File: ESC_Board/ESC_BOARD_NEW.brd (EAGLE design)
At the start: 127.7 x 178 mm, 165 parts, among them J3 AVR_SPI_PROG_3X2NS, U2 ATMEGA328P_TQFP, U4 PCA9685

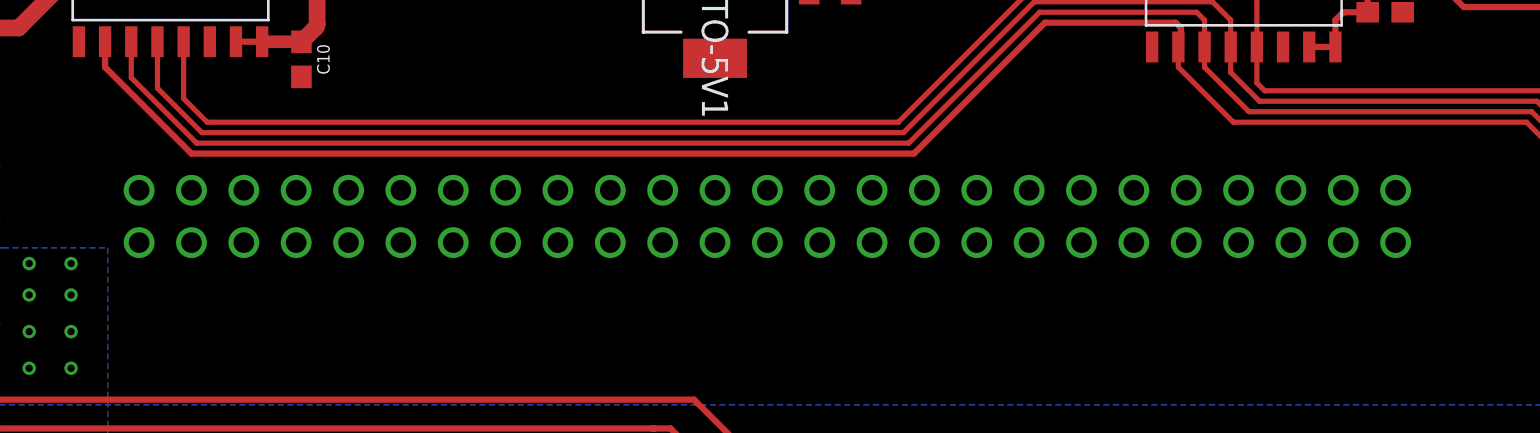
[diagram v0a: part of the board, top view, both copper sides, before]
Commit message: Added standard ESC to power distribution board connector
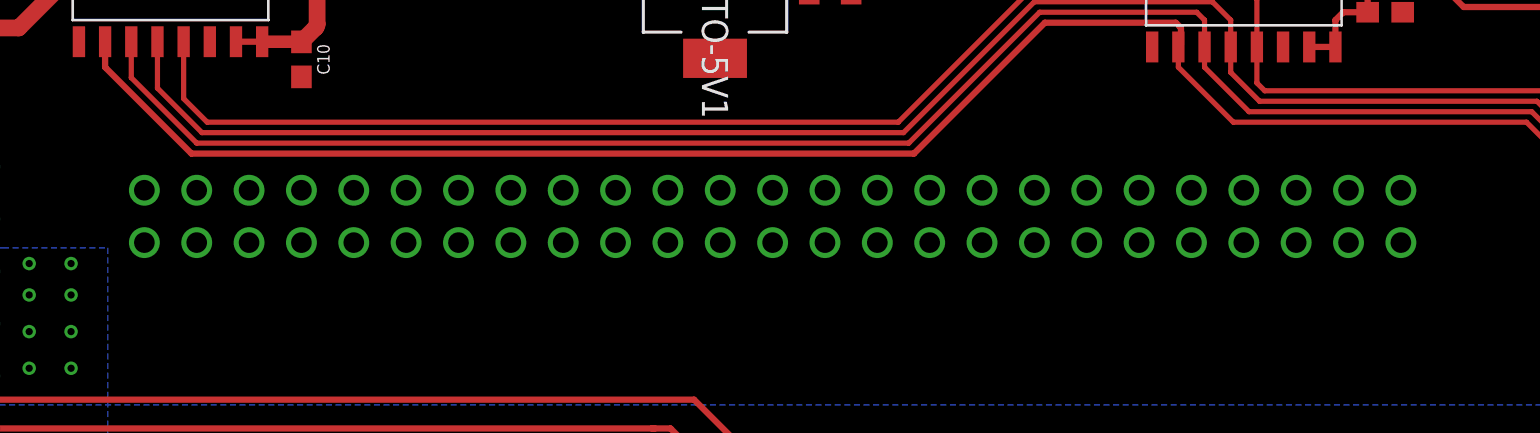
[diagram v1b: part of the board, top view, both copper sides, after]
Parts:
- removed U$17, U$18: POWER-BRICK-CONNECTOR, MotherboardParts:POWER-BRICK-CONNECTOR
- added U$14: ESC-CONNECTORESC-CONNECTOR, MotherboardParts:ESC-CONNECTOR
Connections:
- net +12V: now also U$14.P$100, U$14.P$51, U$14.P$52, U$14.P$53, U$14.P$54, U$14.P$55, U$14.P$56, U$14.P$57, U$14.P$58, U$14.P$59, U$14.P$60, U$14.P$61, U$14.P$62, U$14.P$63, U$14.P$64, U$14.P$65, U$14.P$66, U$14.P$67, U$14.P$68, U$14.P$69, U$14.P$70, U$14.P$71, U$14.P$72, U$14.P$73, U$14.P$74, U$14.P$75, U$14.P$76, U$14.P$77, U$14.P$78, U$14.P$79, U$14.P$80, U$14.P$81, U$14.P$82, U$14.P$83, U$14.P$84, U$14.P$85, U$14.P$86, U$14.P$87, U$14.P$88, U$14.P$89, U$14.P$90, U$14.P$91, U$14.P$92, U$14.P$93, U$14.P$94, U$14.P$95, U$14.P$96, U$14.P$97, U$14.P$98, U$14.P$99; no longer U$18.P$1, U$18.P$10, U$18.P$11, U$18.P$12, U$18.P$13, U$18.P$14, U$18.P$15, U$18.P$16, U$18.P$17, U$18.P$18, U$18.P$19, U$18.P$2, U$18.P$20, U$18.P$21, U$18.P$22, U$18.P$23, U$18.P$24, U$18.P$25, U$18.P$26, U$18.P$27, U$18.P$28, U$18.P$29, U$18.P$3, U$18.P$30, U$18.P$31, U$18.P$32, U$18.P$33, U$18.P$34, U$18.P$35, U$18.P$36, U$18.P$37, U$18.P$38, U$18.P$39, U$18.P$4, U$18.P$40, U$18.P$41, U$18.P$42, U$18.P$43, U$18.P$44, U$18.P$45, U$18.P$46, U$18.P$47, U$18.P$48, U$18.P$49, U$18.P$5, U$18.P$50, U$18.P$6, U$18.P$7, U$18.P$8, U$18.P$9
- net GND: now also U$14.P$1, U$14.P$10, U$14.P$11, U$14.P$12, U$14.P$13, U$14.P$14, U$14.P$15, U$14.P$16, U$14.P$17, U$14.P$18, U$14.P$19, U$14.P$2, U$14.P$20, U$14.P$21, U$14.P$22, U$14.P$23, U$14.P$24, U$14.P$25, U$14.P$26, U$14.P$27, U$14.P$28, U$14.P$29, U$14.P$3, U$14.P$30, U$14.P$31, U$14.P$32, U$14.P$33, U$14.P$34, U$14.P$35, U$14.P$36, U$14.P$37, U$14.P$38, U$14.P$39, U$14.P$4, U$14.P$40, U$14.P$41, U$14.P$42, U$14.P$43, U$14.P$44, U$14.P$45, U$14.P$46, U$14.P$47, U$14.P$48, U$14.P$49, U$14.P$5, U$14.P$50, U$14.P$6, U$14.P$7, U$14.P$8, U$14.P$9; no longer U$17.P$1, U$17.P$10, U$17.P$11, U$17.P$12, U$17.P$13, U$17.P$14, U$17.P$15, U$17.P$16, U$17.P$17, U$17.P$18, U$17.P$19, U$17.P$2, U$17.P$20, U$17.P$21, U$17.P$22, U$17.P$23, U$17.P$24, U$17.P$25, U$17.P$26, U$17.P$27, U$17.P$28, U$17.P$29, U$17.P$3, U$17.P$30, U$17.P$31, U$17.P$32, U$17.P$33, U$17.P$34, U$17.P$35, U$17.P$36, U$17.P$37, U$17.P$38, U$17.P$39, U$17.P$4, U$17.P$40, U$17.P$41, U$17.P$42, U$17.P$43, U$17.P$44, U$17.P$45, U$17.P$46, U$17.P$47, U$17.P$48, U$17.P$49, U$17.P$5, U$17.P$50, U$17.P$6, U$17.P$7, U$17.P$8, U$17.P$9

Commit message: Some final changes
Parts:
- U$14: value ESC-CONNECTORESC-CONNECTOR -> ESC-CONNECTORPARALLELL; device MotherboardParts:ESC-CONNECTOR -> MotherboardParts:ESC-PARALLELL
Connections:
- net +12V: now also U$14.P$101, U$14.P$102, U$14.P$103, U$14.P$104, U$14.P$105, U$14.P$106, U$14.P$107, U$14.P$108, U$14.P$109, U$14.P$110, U$14.P$111, U$14.P$112, U$14.P$113, U$14.P$114, U$14.P$115, U$14.P$116, U$14.P$117, U$14.P$118, U$14.P$119, U$14.P$120, U$14.P$121, U$14.P$122, U$14.P$123, U$14.P$124, U$14.P$125, U$14.P$126, U$14.P$127, U$14.P$128, U$14.P$129, U$14.P$130; no longer U$14.P$100, U$14.P$81, U$14.P$82, U$14.P$83, U$14.P$84, U$14.P$85, U$14.P$86, U$14.P$87, U$14.P$88, U$14.P$89, U$14.P$90, U$14.P$91, U$14.P$92, U$14.P$93, U$14.P$94, U$14.P$95, U$14.P$96, U$14.P$97, U$14.P$98, U$14.P$99
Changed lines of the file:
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@@
 <element name="LED8" library="microbuilder" package="WS2812B" value="WS2812B5050" x="85.852" y="22.352" rot="R270"/>
 <element name="C8" library="rcl" library_urn="urn:adsk.eagle:library:334" package="C0603" package3d_urn="urn:adsk.eagle:package:23616/2" value="0.1uF" x="88.138" y="18.034" rot="MR180"/>
-<element name="U$14" library="MotherboardParts" package="ESC-CONNECTOR" value="ESC-CONNECTORESC-CONNECTOR" x="55.372" y="173.736" rot="R90"/>
+<element name="U$14" library="MotherboardParts" package="ESC-PARALLELL" value="ESC-CONNECTORPARALLELL" x="55.372" y="173.736" rot="R90"/>
 </elements>
 <signals>
@@
 <contactref element="U$16" pad="P$8"/>
 <contactref element="U$16" pad="P$9"/>
-<contactref element="U$14" pad="P$85"/>
+<contactref element="U$14" pad="P$105"/>
 <contactref element="U$14" pad="P$73"/>
 <contactref element="U$14" pad="P$77"/>
@@
 <contactref element="U$14" pad="P$79"/>
 <contactref element="U$14" pad="P$66"/>
-<contactref element="U$14" pad="P$82"/>
-<contactref element="U$14" pad="P$81"/>
+<contactref element="U$14" pad="P$102"/>
+<contactref element="U$14" pad="P$101"/>
 <contactref element="U$14" pad="P$55"/>
 <contactref element="U$14" pad="P$60"/>
-<contactref element="U$14" pad="P$97"/>
-<contactref element="U$14" pad="P$87"/>
-<contactref element="U$14" pad="P$99"/>
-<contactref element="U$14" pad="P$83"/>
+<contactref element="U$14" pad="P$117"/>
+<contactref element="U$14" pad="P$107"/>
+<contactref element="U$14" pad="P$119"/>
+<contactref element="U$14" pad="P$103"/>
 <contactref element="U$14" pad="P$78"/>
-<contactref element="U$14" pad="P$94"/>
-<contactref element="U$14" pad="P$98"/>
+<contactref element="U$14" pad="P$114"/>
+<contactref element="U$14" pad="P$118"/>
 <contactref element="U$14" pad="P$75"/>
 <contactref element="U$14" pad="P$64"/>
-<contactref element="U$14" pad="P$89"/>
+<contactref element="U$14" pad="P$109"/>
 <contactref element="U$14" pad="P$56"/>
-<contactref element="U$14" pad="P$95"/>
+<contactref element="U$14" pad="P$115"/>
 <contactref element="U$14" pad="P$71"/>
 <contactref element="U$14" pad="P$68"/>
-<contactref element="U$14" pad="P$90"/>
+<contactref element="U$14" pad="P$110"/>
 <contactref element="U$14" pad="P$63"/>
-<contactref element="U$14" pad="P$84"/>
+<contactref element="U$14" pad="P$104"/>
 <contactref element="U$14" pad="P$61"/>
 <contactref element="U$14" pad="P$69"/>
-<contactref element="U$14" pad="P$92"/>
-<contactref element="U$14" pad="P$100"/>
+<contactref element="U$14" pad="P$112"/>
+<contactref element="U$14" pad="P$120"/>
 <contactref element="U$14" pad="P$54"/>
-<contactref element="U$14" pad="P$96"/>
+<contactref element="U$14" pad="P$116"/>
 <contactref element="U$14" pad="P$80"/>
 <contactref element="U$14" pad="P$67"/>
@@
 <contactref element="U$14" pad="P$70"/>
 <contactref element="U$14" pad="P$72"/>
-<contactref element="U$14" pad="P$91"/>
+<contactref element="U$14" pad="P$111"/>
 <contactref element="U$14" pad="P$52"/>
 <contactref element="U$14" pad="P$65"/>
-<contactref element="U$14" pad="P$86"/>
+<contactref element="U$14" pad="P$106"/>
 <contactref element="U$14" pad="P$51"/>
-<contactref element="U$14" pad="P$93"/>
-<contactref element="U$14" pad="P$88"/>
+<contactref element="U$14" pad="P$113"/>
+<contactref element="U$14" pad="P$108"/>
+<contactref element="U$14" pad="P$121"/>
+<contactref element="U$14" pad="P$122"/>
+<contactref element="U$14" pad="P$123"/>
+<contactref element="U$14" pad="P$124"/>
+<contactref element="U$14" pad="P$125"/>
+<contactref element="U$14" pad="P$126"/>
+<contactref element="U$14" pad="P$127"/>
+<contactref element="U$14" pad="P$128"/>
+<contactref element="U$14" pad="P$129"/>
+<contactref element="U$14" pad="P$130"/>
 </signal>
 <signal name="PWM2">

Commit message: Added way to power electro magnets
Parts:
- added J4, J6: (no value), SparkFun-Connectors:1X02
- added LED10, LED9: (no value), led:SML0603
- added R4, R5: 330, resistor:R0603
- added U1, U3: FQB27P06, CamSensComponents:TO263-3
- moved P7 3.75 mm to (3.81, 35.3)
- moved P6 1.48 mm to (3.81, 37.8)
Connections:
- removed net PWME1: P6.1, U4.12
- removed net PWME2: P7.1, U4.13
- new net E_MAG_1: J4.2, R5.2, U1.TAB
- new net E_MAG_1_ON: P6.1, U1.1, U4.12
- new net E_MAG_2: J6.2, R4.2, U3.TAB
- new net E_MAG_2_ON: P7.1, U3.1, U4.13
- new net N$51: LED9.A, R5.1
- new net N$64: LED10.A, R4.1
- net +12V: now also U1.3, U3.3
- net GND: now also J4.1, J6.1, LED10.C, LED9.C
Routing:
- net E_MAG_1_ON: track 0.00 -> 83.0 mm, vias 0 -> 1
- net E_MAG_2_ON: track 0.00 -> 74.9 mm
- net E_MAG_1: track 0.00 -> 32.2 mm
- net E_MAG_2: track 0.00 -> 20.1 mm
- net PWME2: track 8.69 -> 0.00 mm
- net PWME1: track 6.06 -> 0.00 mm
- net +12V: track 0.00 -> 2.29 mm, vias 11 -> 12
- net N$51: track 0.00 -> 1.96 mm
- net N$64: track 0.00 -> 1.70 mm
- net MOSI: track 162.5 -> 161.6 mm
- net +5V: track 766.0 -> 765.1 mm
- net GND: vias 96 -> 105

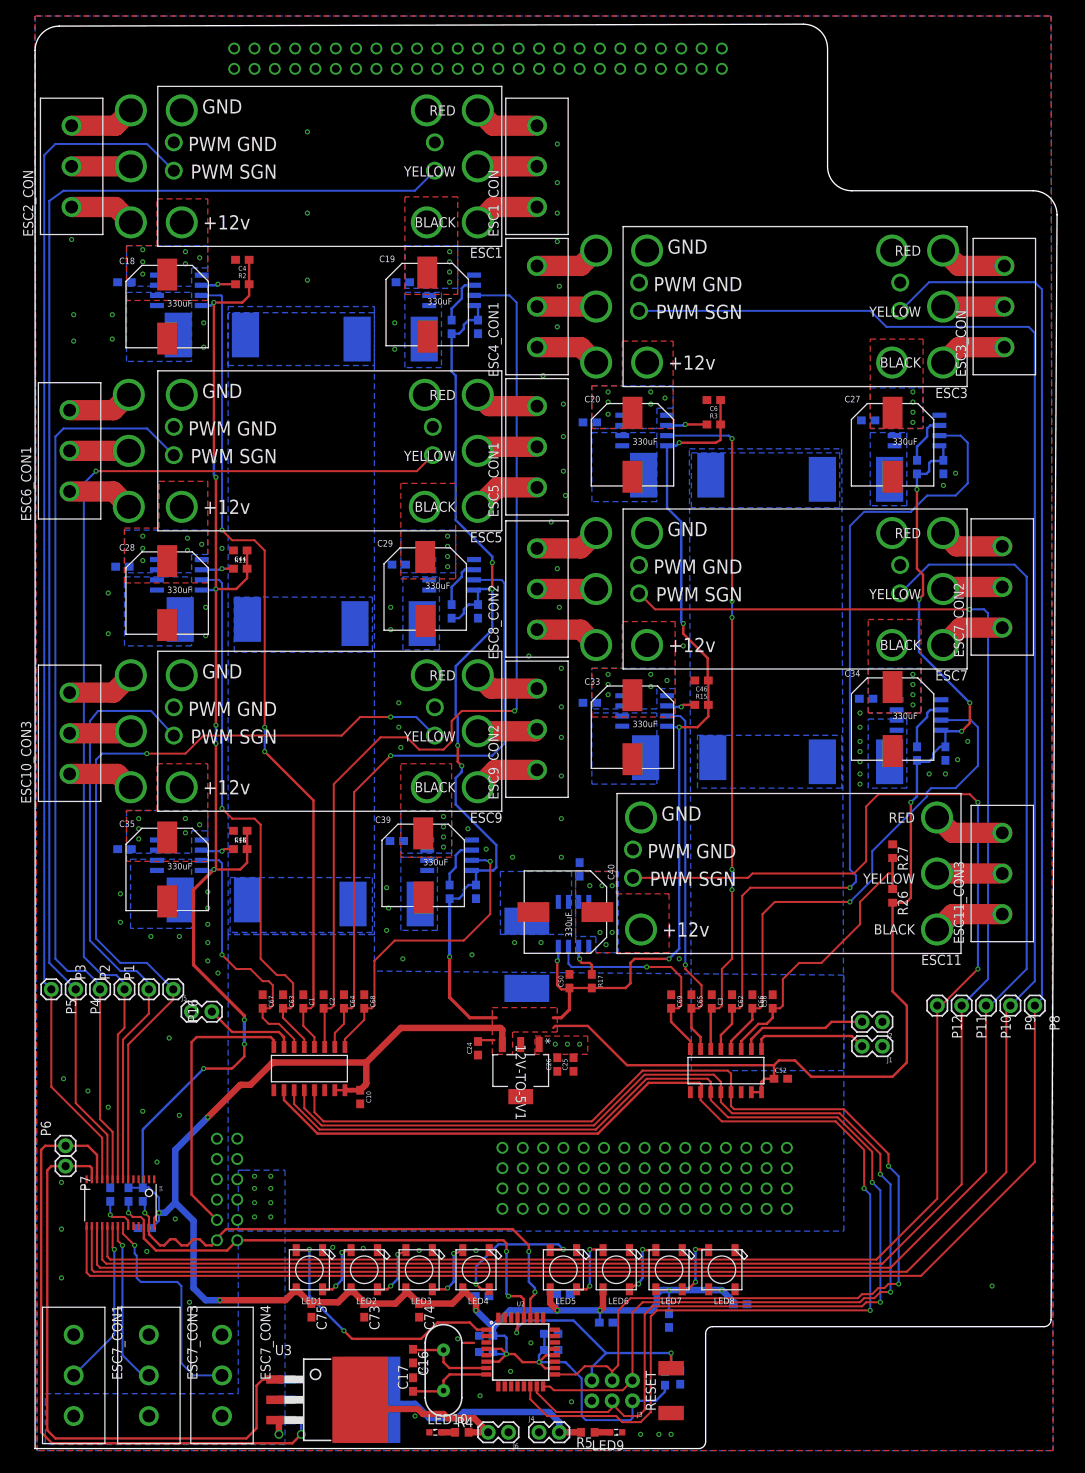
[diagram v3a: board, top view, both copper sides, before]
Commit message: fixed up some of ground plane
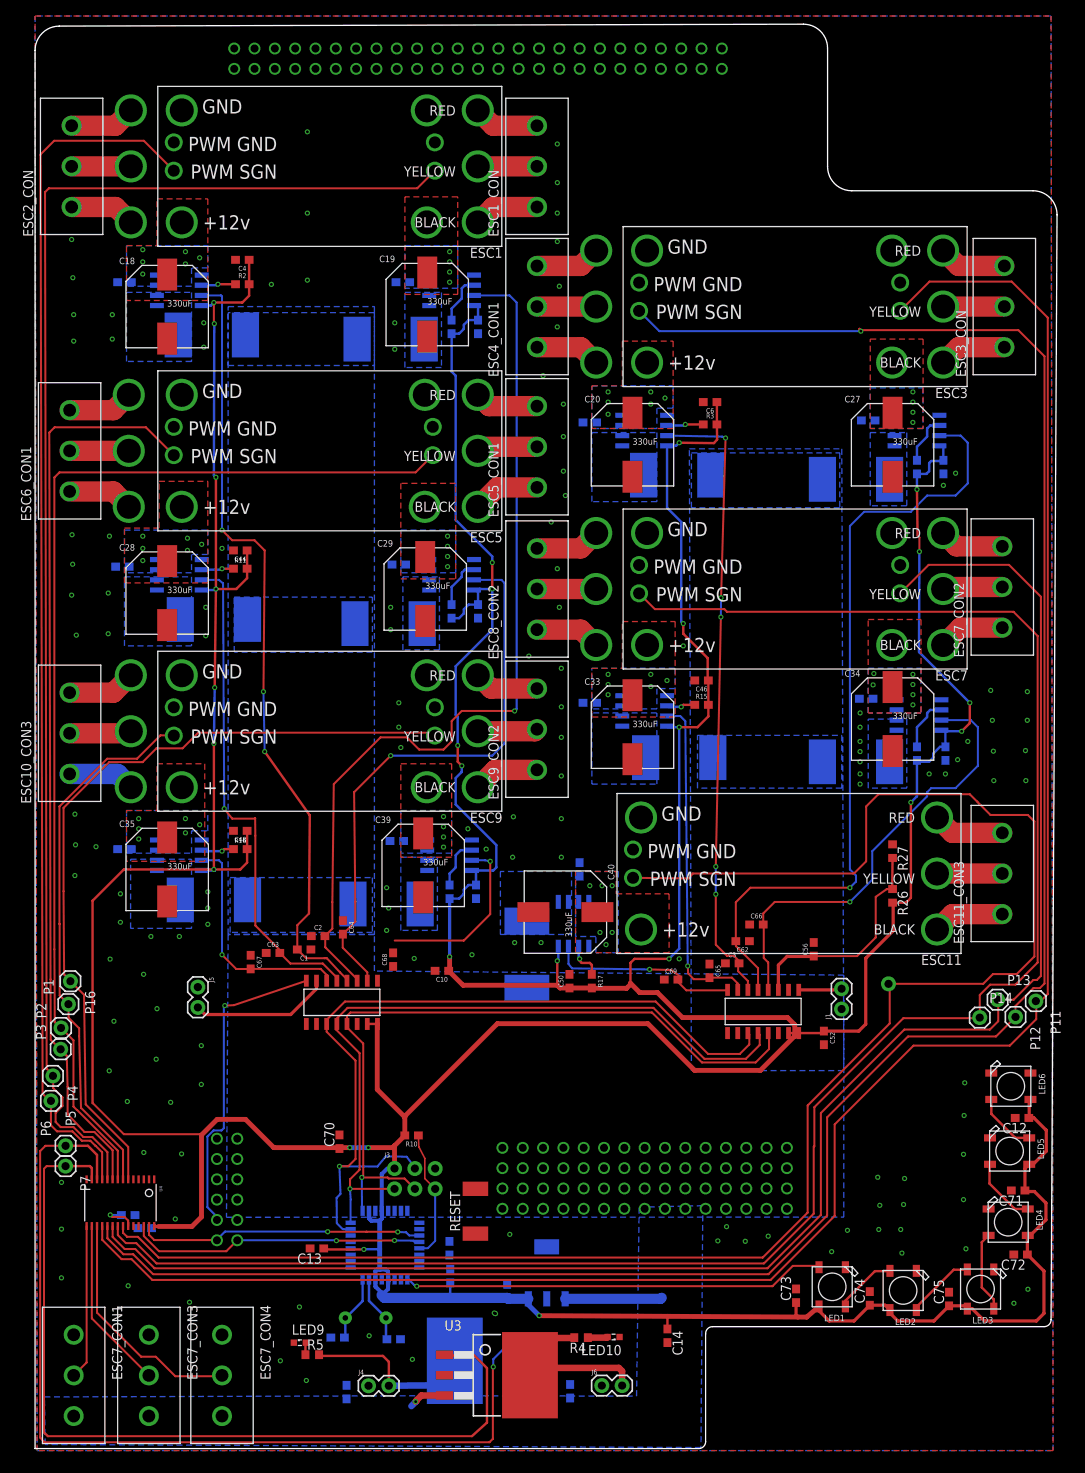
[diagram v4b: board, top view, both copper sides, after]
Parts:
- removed C7, C8: 0.1uF, rcl:C0603
- removed J2: (no value), SparkFun-Connectors:1X02
- removed LED7, LED8: WS2812B5050, microbuilder:WS2812B
- removed P10, P8, P9: (no value), SparkFun-Connectors:1X01
- removed R20, R21: 10k, SparkFun-Resistors:0603-RES
- added P13, P14, P15: (no value), SparkFun-Connectors:1X01
- moved C75 79.7 mm to (114.2, 18.7), turned to 90 degrees
- moved C12 72.3 mm to (123.4, 41.3), flipped to the top, turned to 180 degrees
- moved LED3 70.2 mm to (118.2, 19.9)
- moved C71 68.3 mm to (122.9, 32.3), flipped to the top
- moved LED2 67.4 mm to (108.5, 19.8)
- moved LED4 66.8 mm to (121.6, 28.3), turned to 0 degrees
- moved LED1 65.4 mm to (99.6, 20.2)
- moved LED5 57.7 mm to (121.8, 37.2), turned to 0 degrees
- moved C74 56.4 mm to (104.3, 18.8), turned to 90 degrees
- moved LED6 54.4 mm to (122.0, 45.3), turned to 0 degrees
- moved C73 54.0 mm to (95.1, 19.1), turned to 90 degrees
- moved C72 52.5 mm to (123.2, 24.3), flipped to the top
- moved C25 49.8 mm to (38.9, 7.06), flipped to the bottom, turned to 270 degrees
- moved R10 43.9 mm to (47.1, 39.1), flipped to the top, turned to 180 degrees
- moved LED9 41.1 mm to (33.1, 13.2), turned to 0 degrees
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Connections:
- removed net OUT7: LED7.2-DOUT, LED8.4-DIN
- removed net OUT8: LED8.2-DOUT
- net +5V: no longer C7.1, C8.1, LED7.1-VDD, LED8.1-VDD, R20.2, R21.2
- net E4: no longer J2.2
- net GND: no longer C7.2, C8.2, J2.1, LED7.3-GND, LED8.3-GND
- net LED1: now also U4.15; no longer U4.20
- net LED2: now also U4.16; no longer U4.21
- net OUT6: no longer LED7.4-DIN
- net PIEZO: now also U4.17; no longer U4.22
- net PWM11: now also P15.1, U4.22; no longer P12.1, U4.19
- net PWM3: now also P12.1, U4.19; no longer P9.1, U4.16
- net PWM4: now also P11.1, U4.18; no longer P8.1, U4.15
- net PWM7: now also P14.1, U4.21; no longer P11.1, U4.18
- net PWM8: now also P13.1, U4.20; no longer P10.1, U4.17
- net SCL: no longer R21.1
- net SDA: no longer R20.1
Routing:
- net CS: track 161.6 -> 0.00 mm, vias 2 -> 0
- net MISO: track 155.1 -> 91.3 mm, vias 2 -> 1
- net SCK: track 154.4 -> 91.1 mm, vias 2 -> 1
- net MOSI: track 161.6 -> 100.1 mm, vias 2 -> 1
- net E_MAG_1_ON: track 83.0 -> 120.6 mm
- net E_MAG_2_ON: track 74.9 -> 109.6 mm
- net SDA: track 65.3 -> 35.9 mm, vias 3 -> 2
- net +5V: track 765.1 -> 792.1 mm, vias 35 -> 26
- net SCL: track 63.9 -> 37.1 mm, vias 3 -> 2
- net PD3: track 33.1 -> 52.9 mm, vias 2 -> 1
- net +12V: track 2.29 -> 20.5 mm, vias 12 -> 1
- net RESET: track 34.0 -> 16.3 mm, vias 2 -> 0
- net CUR10: track 38.6 -> 22.2 mm
- net E4: track 16.0 -> 0.00 mm
- net E_MAG_1: track 32.2 -> 21.6 mm
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- removed copper zone on layer 1, net +12V
- removed copper zone on layer 1, net +5V

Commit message: Fixing gnd plane and fixing traces
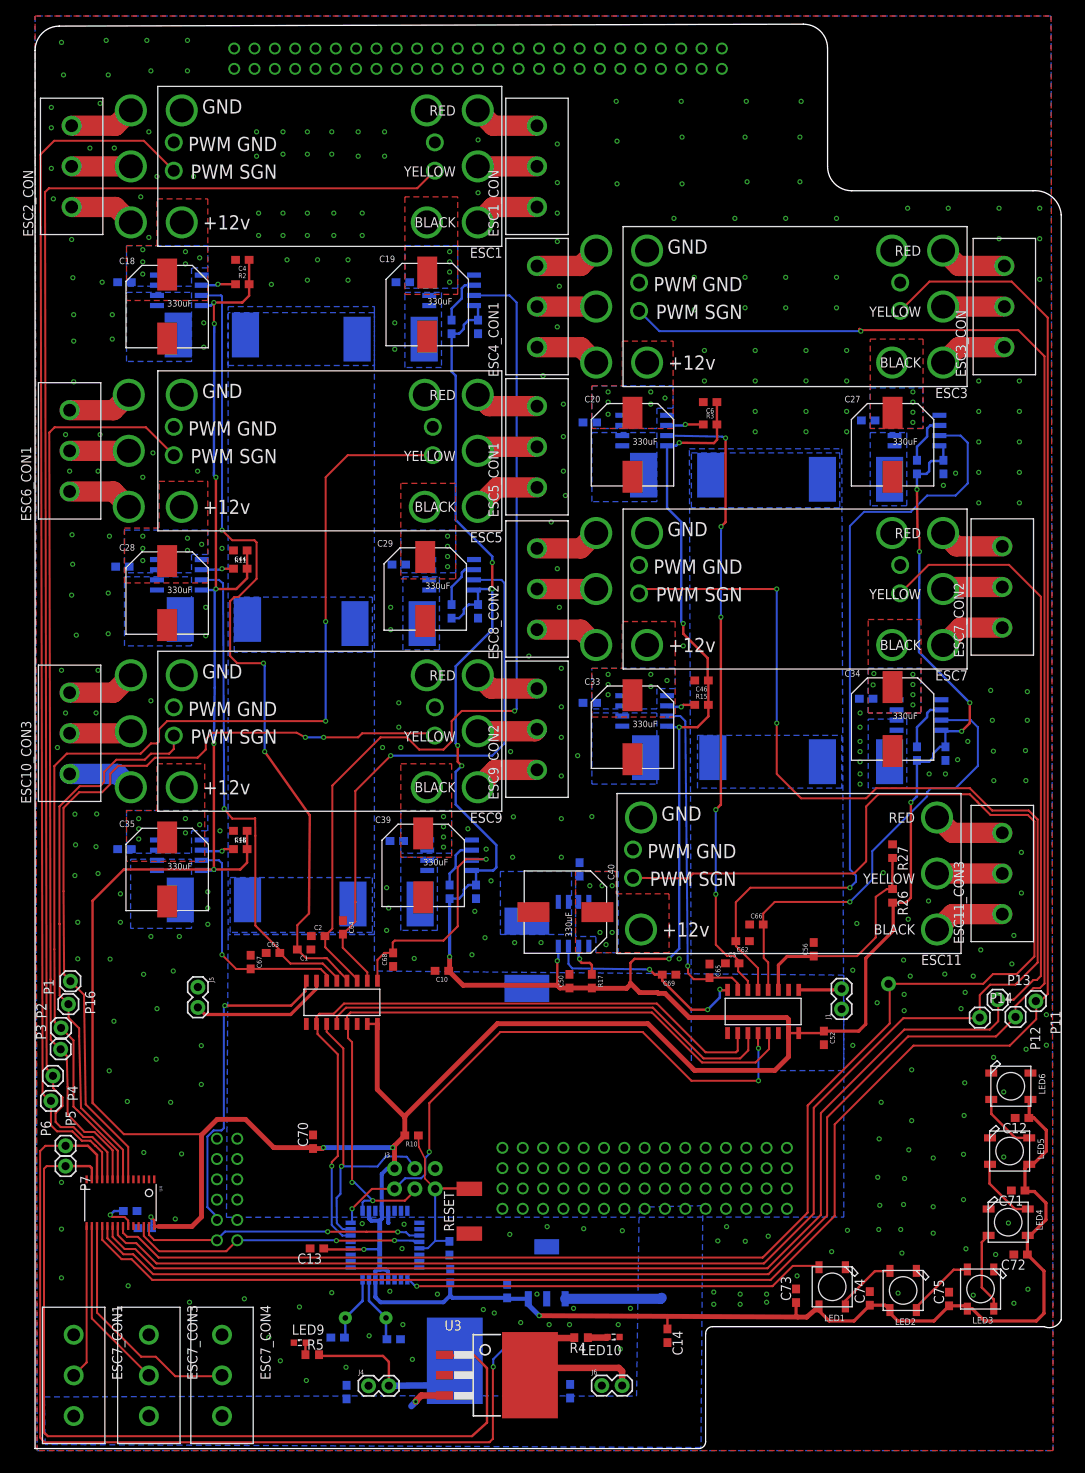
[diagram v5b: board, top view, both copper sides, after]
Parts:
- moved C70 3.30 mm to (34.7, 38.4)
- moved RESET 0.76 mm to (54.3, 29.7)
- moved C69 0.66 mm to (79.2, 59.2), turned to 180 degrees
- moved R19 0.57 mm to (11.9, 29.7)
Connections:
- new net TEMP1: U$13.DIN, U$4.DOUT
- net MISO: no longer U$4.DOUT
- net MOSI: no longer U$13.DIN
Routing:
- net CS: track 0.00 -> 88.5 mm, vias 0 -> 1
- net MOSI: track 100.1 -> 38.7 mm
- net TEMP1: track 0.00 -> 58.1 mm
- net MISO: track 91.3 -> 75.2 mm, vias 1 -> 4
- net RESET: track 16.3 -> 23.5 mm
- net CUR10: track 22.2 -> 28.3 mm
- net CUR1: track 98.4 -> 103.3 mm
- net CUR11: track 23.8 -> 26.5 mm, vias 1 -> 3
- net PWM6: track 139.5 -> 137.1 mm, vias 0 -> 2
- net PWM10: track 100.1 -> 101.9 mm, vias 0 -> 2
- net PWM9: track 67.8 -> 69.5 mm
- net PWM7: track 235.4 -> 237.0 mm, vias 0 -> 2
- net GND: track 0.00 -> 1.55 mm, vias 141 -> 336
- net 48_I_ANALOG: track 39.5 -> 41.0 mm
- net +5V: track 792.1 -> 793.5 mm
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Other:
- board size 127.7 x 178 mm -> 128.3 x 178 mm
